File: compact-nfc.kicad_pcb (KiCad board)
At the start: 2 copper layers, 50 x 50 mm, 15 parts, among them U1 ITR9702, U2 PN5321A3HN_C1xx

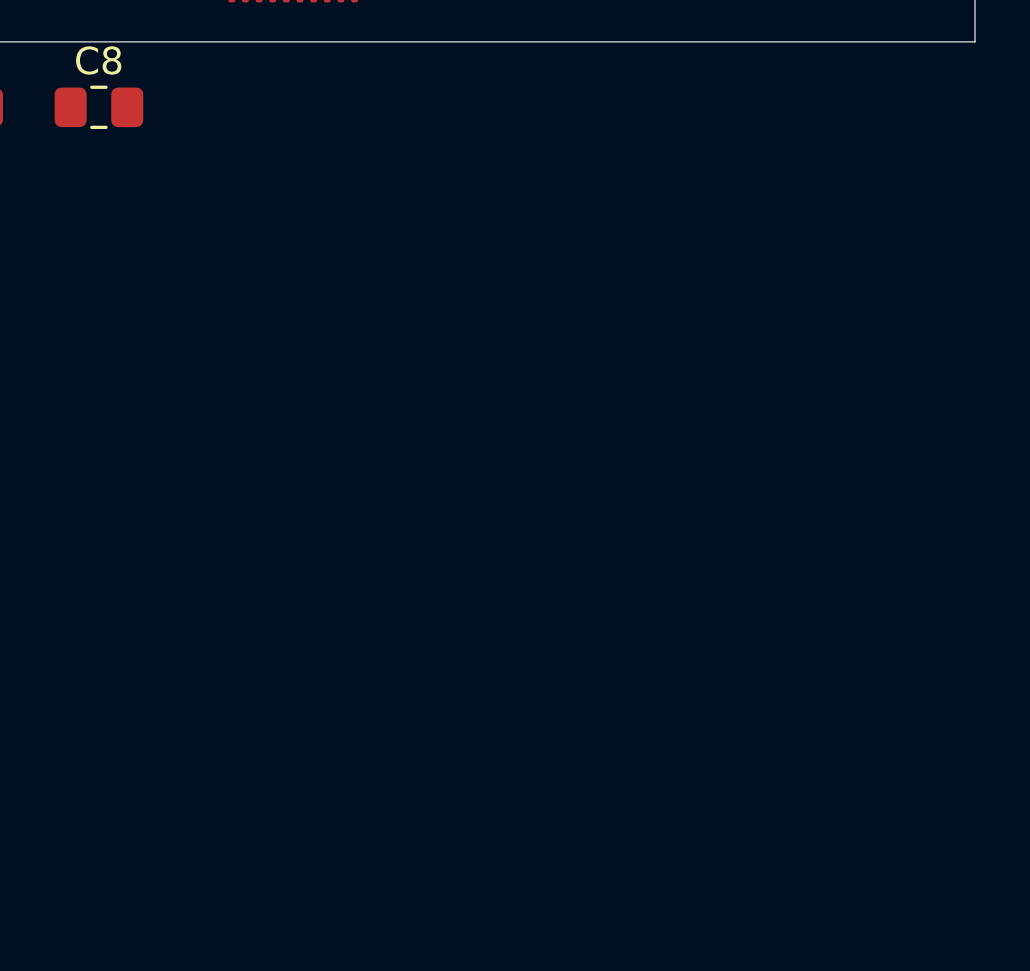
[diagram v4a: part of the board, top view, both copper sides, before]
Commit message: Add more components from reference schematic
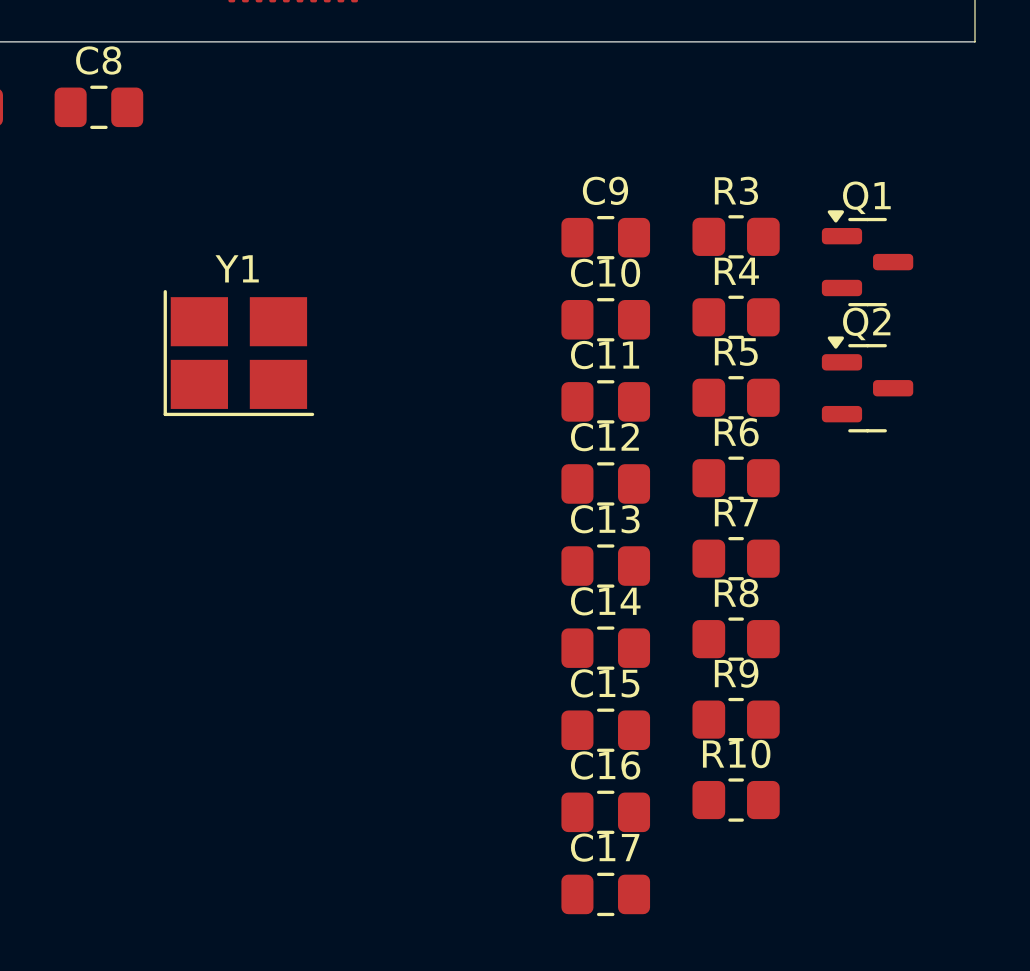
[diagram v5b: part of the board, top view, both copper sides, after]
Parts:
- added C10: C, Capacitor_SMD:C_0805_2012Metric_Pad1.18x1.45mm_HandSolder, F.Cu at (136.5, 160.2)
- added C11: C, Capacitor_SMD:C_0805_2012Metric_Pad1.18x1.45mm_HandSolder, F.Cu at (136.5, 163.2)
- added C12: C, Capacitor_SMD:C_0805_2012Metric_Pad1.18x1.45mm_HandSolder, F.Cu at (136.5, 166.2)
- added C13: C, Capacitor_SMD:C_0805_2012Metric_Pad1.18x1.45mm_HandSolder, F.Cu at (136.5, 169.2)
- added C14: C, Capacitor_SMD:C_0805_2012Metric_Pad1.18x1.45mm_HandSolder, F.Cu at (136.5, 172.2)
- added C15: C, Capacitor_SMD:C_0805_2012Metric_Pad1.18x1.45mm_HandSolder, F.Cu at (136.5, 175.2)
- added C16: C, Capacitor_SMD:C_0805_2012Metric_Pad1.18x1.45mm_HandSolder, F.Cu at (136.5, 178.2)
- added C17: C, Capacitor_SMD:C_0805_2012Metric_Pad1.18x1.45mm_HandSolder, F.Cu at (136.5, 181.3)
- added C9: C, Capacitor_SMD:C_0805_2012Metric_Pad1.18x1.45mm_HandSolder, F.Cu at (136.5, 157.2)
- added Q1: 2N7002, Package_TO_SOT_SMD:SOT-23, F.Cu at (146.1, 158.1)
- added Q2: 2N7002, Package_TO_SOT_SMD:SOT-23, F.Cu at (146.1, 162.7)
- added R10: R, Resistor_SMD:R_0805_2012Metric_Pad1.20x1.40mm_HandSolder, F.Cu at (141.2, 177.8)
- added R3: R, Resistor_SMD:R_0805_2012Metric_Pad1.20x1.40mm_HandSolder, F.Cu at (141.2, 157.2)
- added R4: R, Resistor_SMD:R_0805_2012Metric_Pad1.20x1.40mm_HandSolder, F.Cu at (141.2, 160.1)
- added R5: R, Resistor_SMD:R_0805_2012Metric_Pad1.20x1.40mm_HandSolder, F.Cu at (141.2, 163.1)
- added R6: R, Resistor_SMD:R_0805_2012Metric_Pad1.20x1.40mm_HandSolder, F.Cu at (141.2, 166.0)
- added R7: R, Resistor_SMD:R_0805_2012Metric_Pad1.20x1.40mm_HandSolder, F.Cu at (141.2, 168.9)
- added R8: R, Resistor_SMD:R_0805_2012Metric_Pad1.20x1.40mm_HandSolder, F.Cu at (141.2, 171.9)
- added R9: R, Resistor_SMD:R_0805_2012Metric_Pad1.20x1.40mm_HandSolder, F.Cu at (141.2, 174.8)
- added Y1: Crystal_GND24, Crystal:Crystal_SMD_3225-4Pin_3.2x2.5mm_HandSoldering, F.Cu at (123.0, 161.4)
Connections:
- U2 pad 14: unconnected-(U2-OSCIN-Pad14) -> Net-(U2-OSCIN)
- U2 pad 15: unconnected-(U2-OSCOUT-Pad15) -> Net-(U2-OSCOUT)
- U2 pad 16: unconnected-(U2-I0-Pad16) -> Net-(U2-I0)
- U2 pad 17: unconnected-(U2-I1-Pad17) -> Net-(U2-I1)
- U2 pad 23: unconnected-(U2-PVDD-Pad23) -> +3.3V
- U2 pad 27: unconnected-(U2-NSS/P50_SCL/HSU_RX-Pad27) -> Net-(Q1-S)
- U2 pad 28: unconnected-(U2-MOSI/SDA/HSU_TX-Pad28) -> Net-(Q2-S)
- U2 pad 38: unconnected-(U2-~{RSTPD}-Pad38) -> Net-(U2-~{RSTPD})
- U2 pad 39: unconnected-(U2-DVDD-Pad39) -> +3.3V
- U2 pad 40: unconnected-(U2-VBAT-Pad40) -> VCC
- U2 pad 5: unconnected-(U2-TVDD-Pad5) -> +3.3V
- U2 pad 8: unconnected-(U2-AVDD-Pad8) -> +3.3V

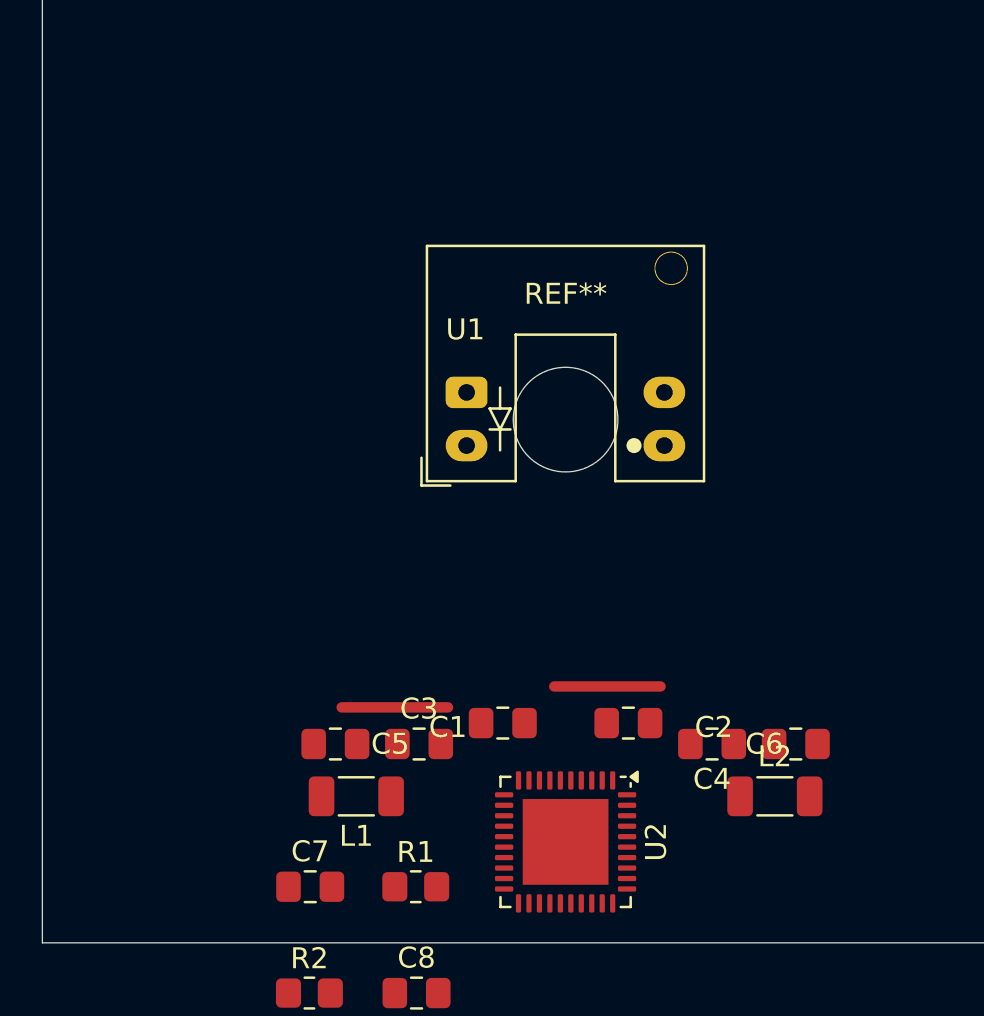
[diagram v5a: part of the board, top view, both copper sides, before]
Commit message: Start coil construction on PCB
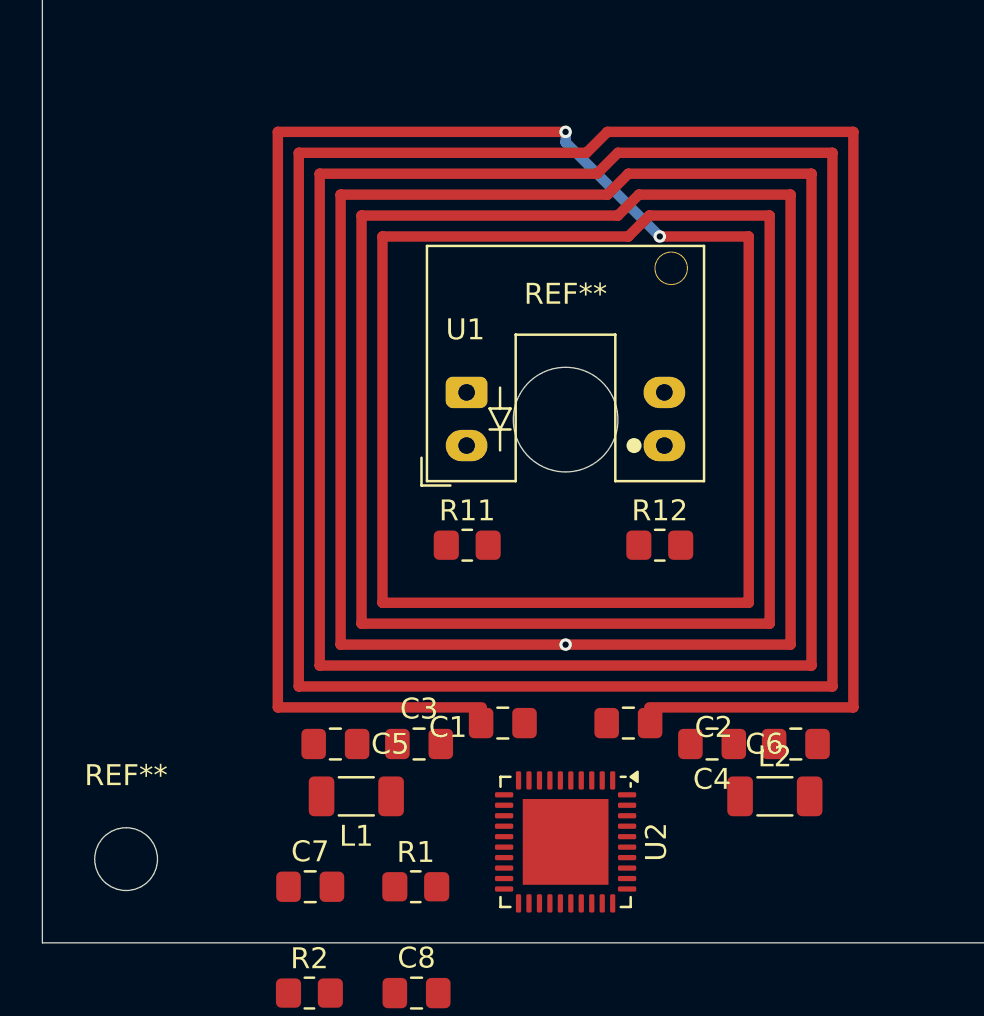
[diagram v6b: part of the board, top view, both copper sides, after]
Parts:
- added R11: R, Resistor_SMD:R_0805_2012Metric_Pad1.20x1.40mm_HandSolder, F.Cu at (120.3, 131.0)
- added R12: R, Resistor_SMD:R_0805_2012Metric_Pad1.20x1.40mm_HandSolder, F.Cu at (129.5, 131.0)
- added REF**: MountingHole_3mm, MountingHole:MountingHole_3mm, F.Cu at (104.0, 146.0)
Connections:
- C2 pad 2: Net-(C2-Pad2) -> Net-(C1-Pad1)
- C4 pad 2: Net-(C2-Pad2) -> Net-(C1-Pad1)
- U1 pad 1: unconnected-(U1-Pad1) -> Net-(R11-Pad2)
- U1 pad 2: unconnected-(U1-Pad2) -> GND
- U1 pad 3: unconnected-(U1-Pad3) -> Net-(R12-Pad1)
- U1 pad 4: unconnected-(U1-Pad4) -> GND
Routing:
- net (no net): track 10.2 -> 441.4 mm, vias 0 -> 3
- net Net-(C1-Pad1): track 0.00 -> 37.2 mm

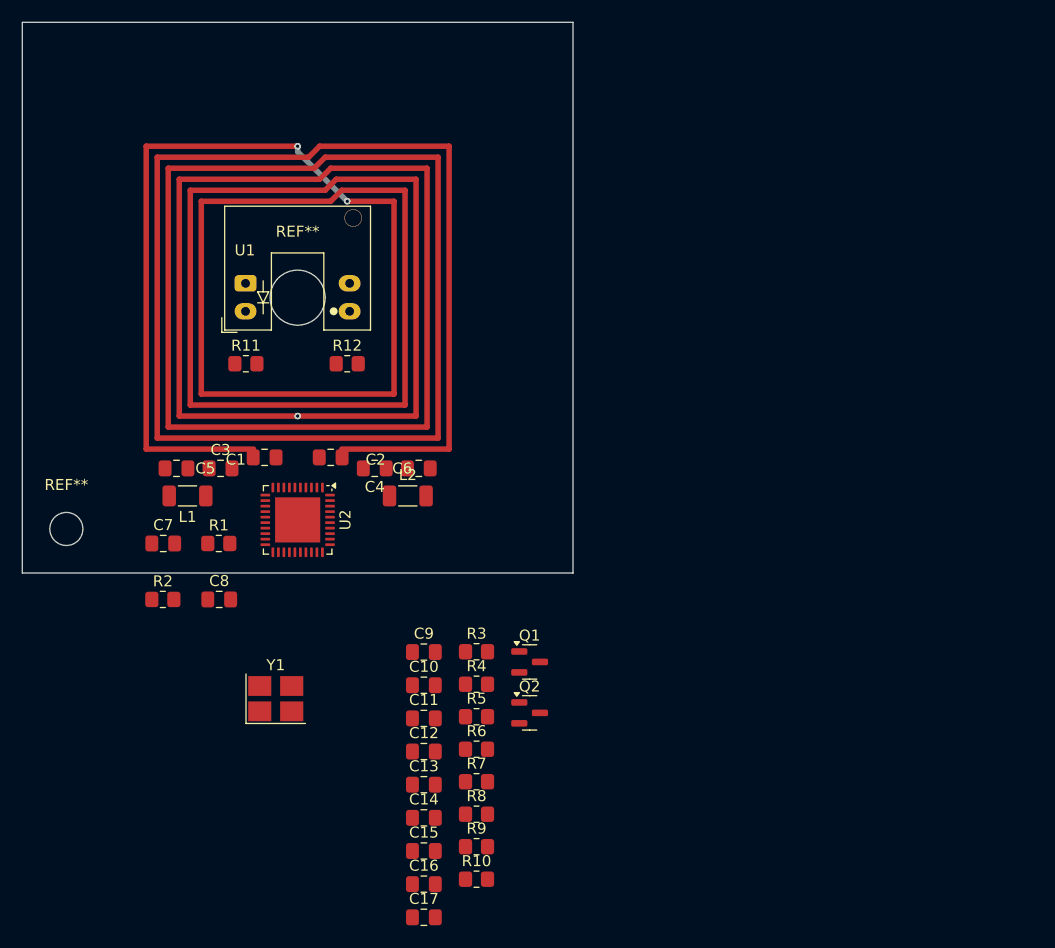
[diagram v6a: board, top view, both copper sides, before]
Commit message: Add coil as PCB library component
- Add L_NFC_PCB footprint (Inductor_PCB.pretty)
- Add coil_pcb symbol
- Update fp-lib-table and sym-lib-table
- Update PCB and schematic with coil placement
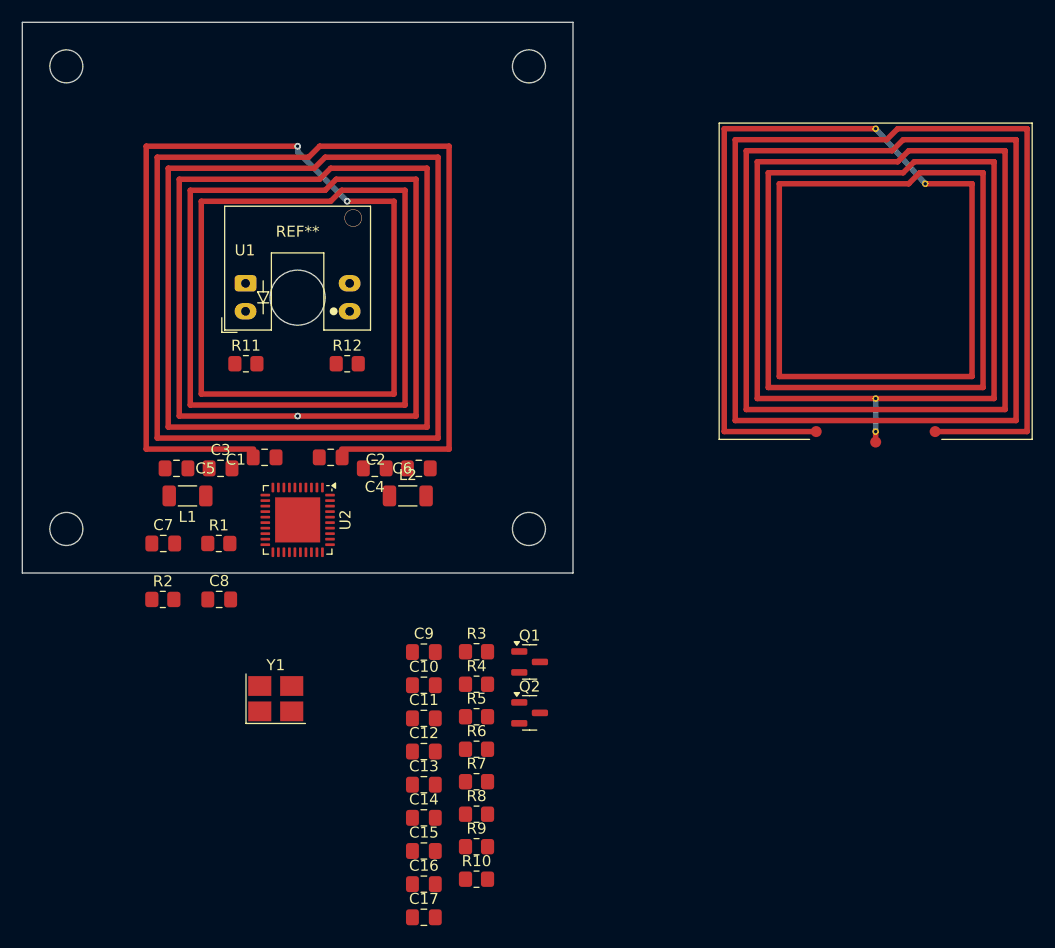
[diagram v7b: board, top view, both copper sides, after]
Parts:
- added L_pcb1: L_pcb, Inductor_PCB:L_NFC_PCB, F.Cu at (177.5, 123.4)
- added REF**: MountingHole_3mm, MountingHole:MountingHole_3mm, F.Cu at (146.0, 146.0)
- added REF**: MountingHole_3mm, MountingHole:MountingHole_3mm, F.Cu at (146.0, 104.0)
- added REF**: MountingHole_3mm, MountingHole:MountingHole_3mm, F.Cu at (104.0, 104.0)
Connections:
- C2 pad 2: Net-(C1-Pad1) -> Net-(C2-Pad2)
- C4 pad 2: Net-(C1-Pad1) -> Net-(C2-Pad2)
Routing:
- net Net-(C2-Pad2): track 0.00 -> 37.2 mm
- net Net-(C1-Pad1): track 37.2 -> 0.00 mm

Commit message: Start clock crystal placement on PCB
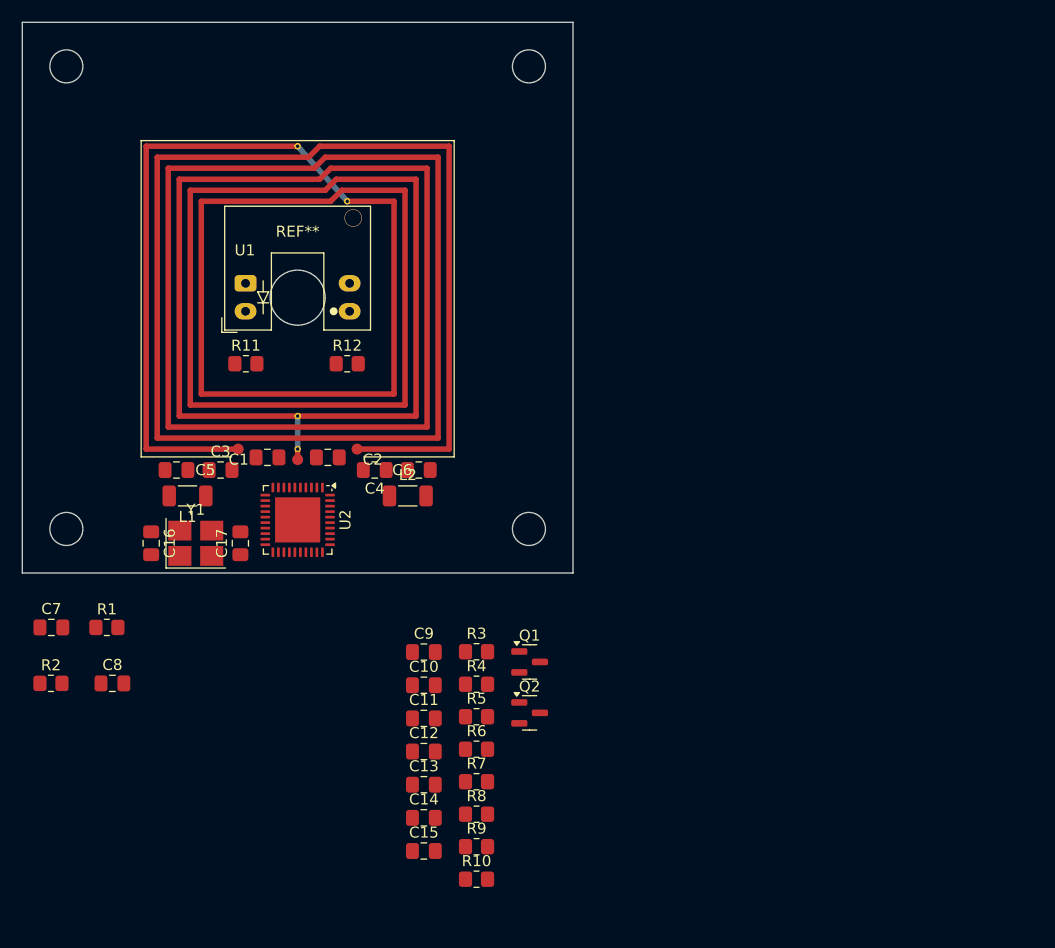
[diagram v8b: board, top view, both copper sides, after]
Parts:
- moved L_pcb1 52.5 mm to (125.0, 125.0)
- moved C16 39.6 mm to (111.7, 147.3), turned to -90 degrees
- moved C17 37.8 mm to (119.8, 147.3), turned to 90 degrees
- moved Y1 15.9 mm to (115.8, 147.3)
- moved R2 12.7 mm to (102.6, 160.0)
- moved C7 12.7 mm to (102.6, 154.9)
- moved R1 12.7 mm to (107.7, 154.9)
- moved C8 12.3 mm to (108.2, 160.0)
- moved C1 0.26 mm to (122.3, 139.5)
- moved C2 0.26 mm to (127.7, 139.5)
- moved C3 0.15 mm to (118.0, 140.7)
- moved C4 0.15 mm to (132.0, 140.7)
- moved C5 0.15 mm to (114.0, 140.7)
- moved C6 0.15 mm to (136.0, 140.7)
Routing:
- net (no net): track 441.4 -> 0.00 mm, vias 3 -> 0
- net Net-(C2-Pad2): track 37.2 -> 0.00 mm
